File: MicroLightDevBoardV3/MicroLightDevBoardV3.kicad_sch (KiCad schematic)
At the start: 34 parts, among them J1 TYPE-C-31-M-12, J3 Conn_01x03_Socket, J4 Conn_01x01_Socket, J5 Conn_01x01_Socket, J6 Conn_01x04_Socket, SW1 SW_Push, U1 USBLC6-2P6, U2 STM32C071GBUx, U3 BQ25180, U4 S-85S1AB33-I6T1U, U5 DF53-2S-0.6H, U7 MC3479

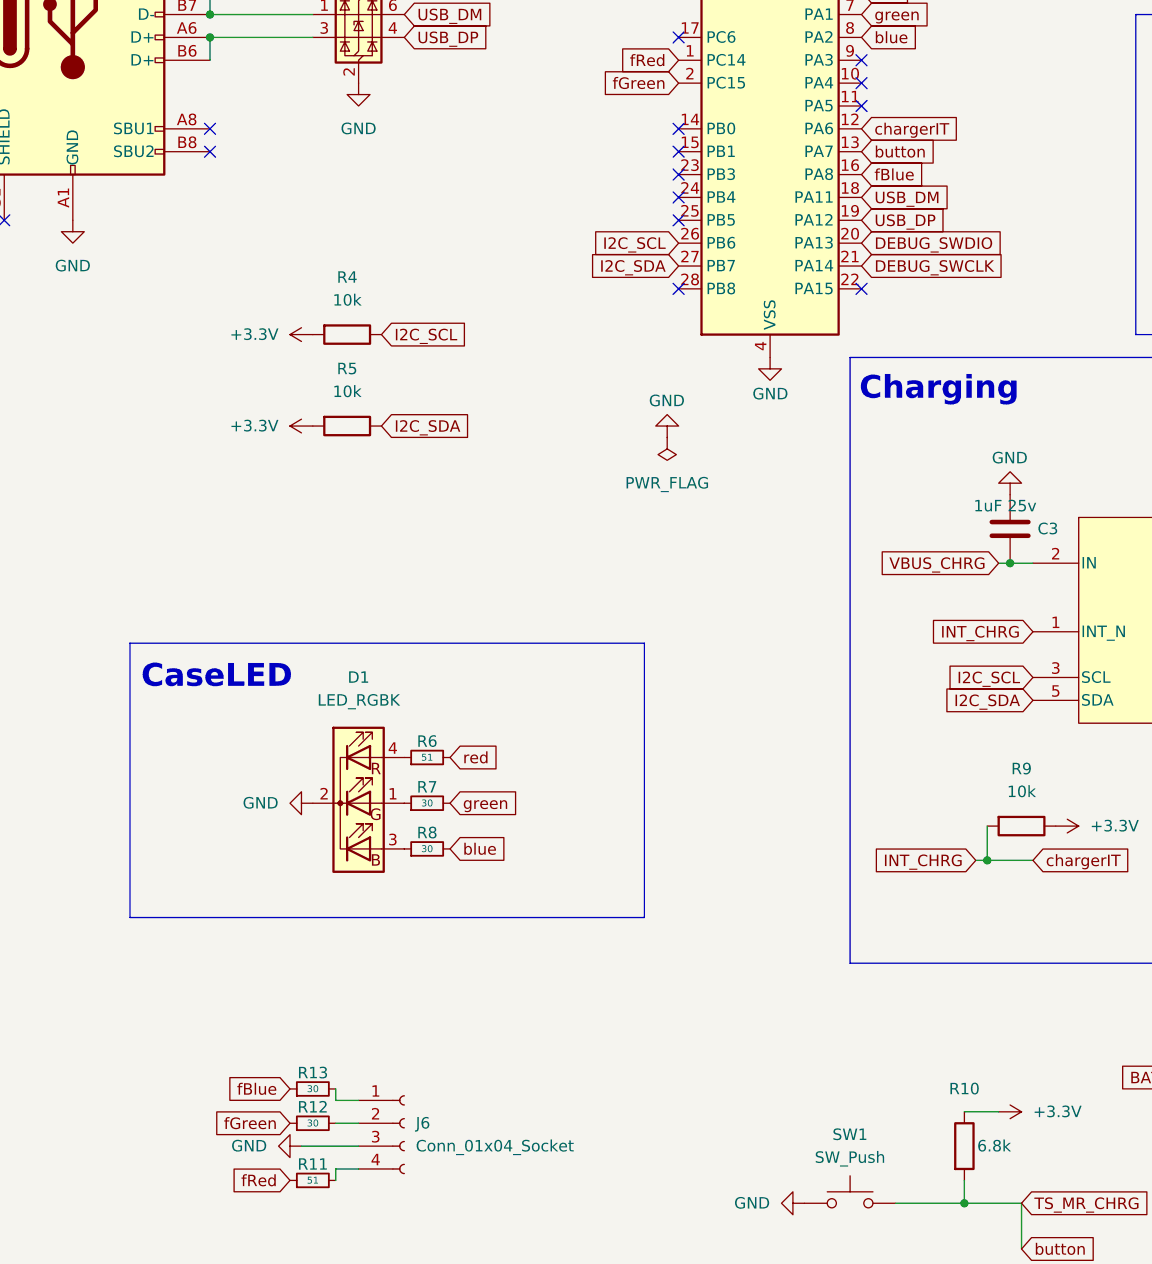
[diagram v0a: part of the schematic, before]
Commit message: rename fBlue to fBlueBulb as it controls power for blue in rgb led, as well as power for 2 pin bulb leds
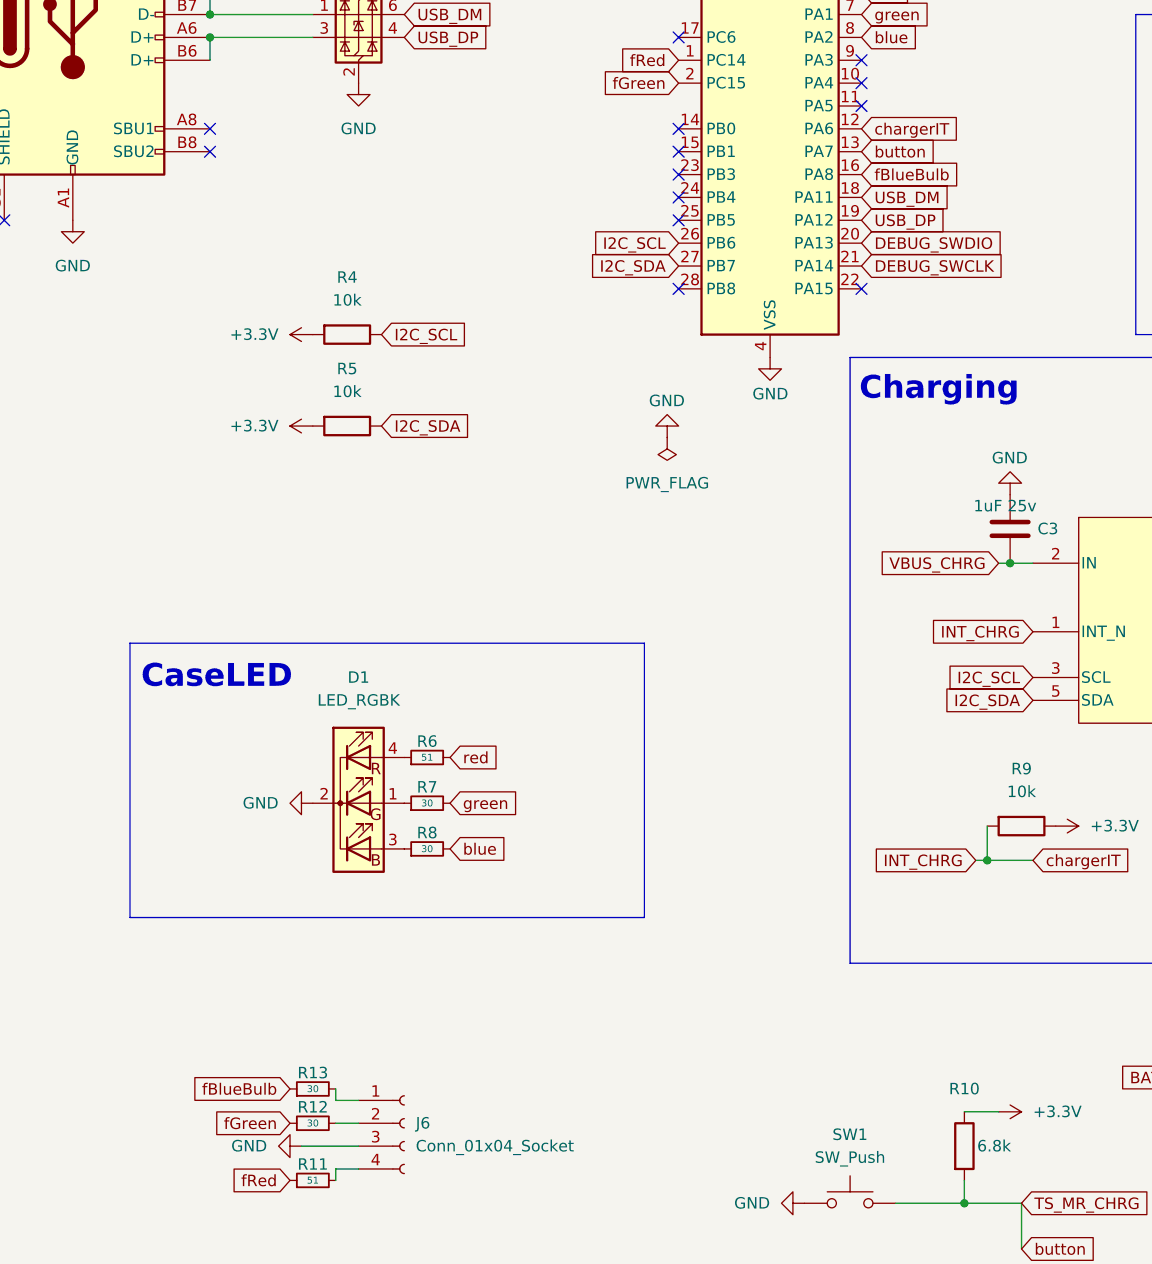
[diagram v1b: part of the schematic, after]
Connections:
- net fBlue renamed fBlueBulb
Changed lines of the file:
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@@
 		)
 	)
-	(global_label "fBlue"
+	(global_label "fBlueBulb"
 		(shape input)
 		(at 114.3 58.42 0)
@@
 		)
 		(property "Intersheetrefs" "${INTERSHEET_REFS}"
-			(at 122.1837 58.42 0)
+			(at 126.4169 58.42 0)
 			(effects
 				(font
@@
 		)
 	)
-	(global_label "fBlue"
+	(global_label "fBlueBulb"
 		(shape input)
 		(at 50.8 160.02 180)
@@
 		)
 		(property "Intersheetrefs" "${INTERSHEET_REFS}"
-			(at 42.9163 160.02 0)
+			(at 38.6831 160.02 0)
 			(effects
 				(font

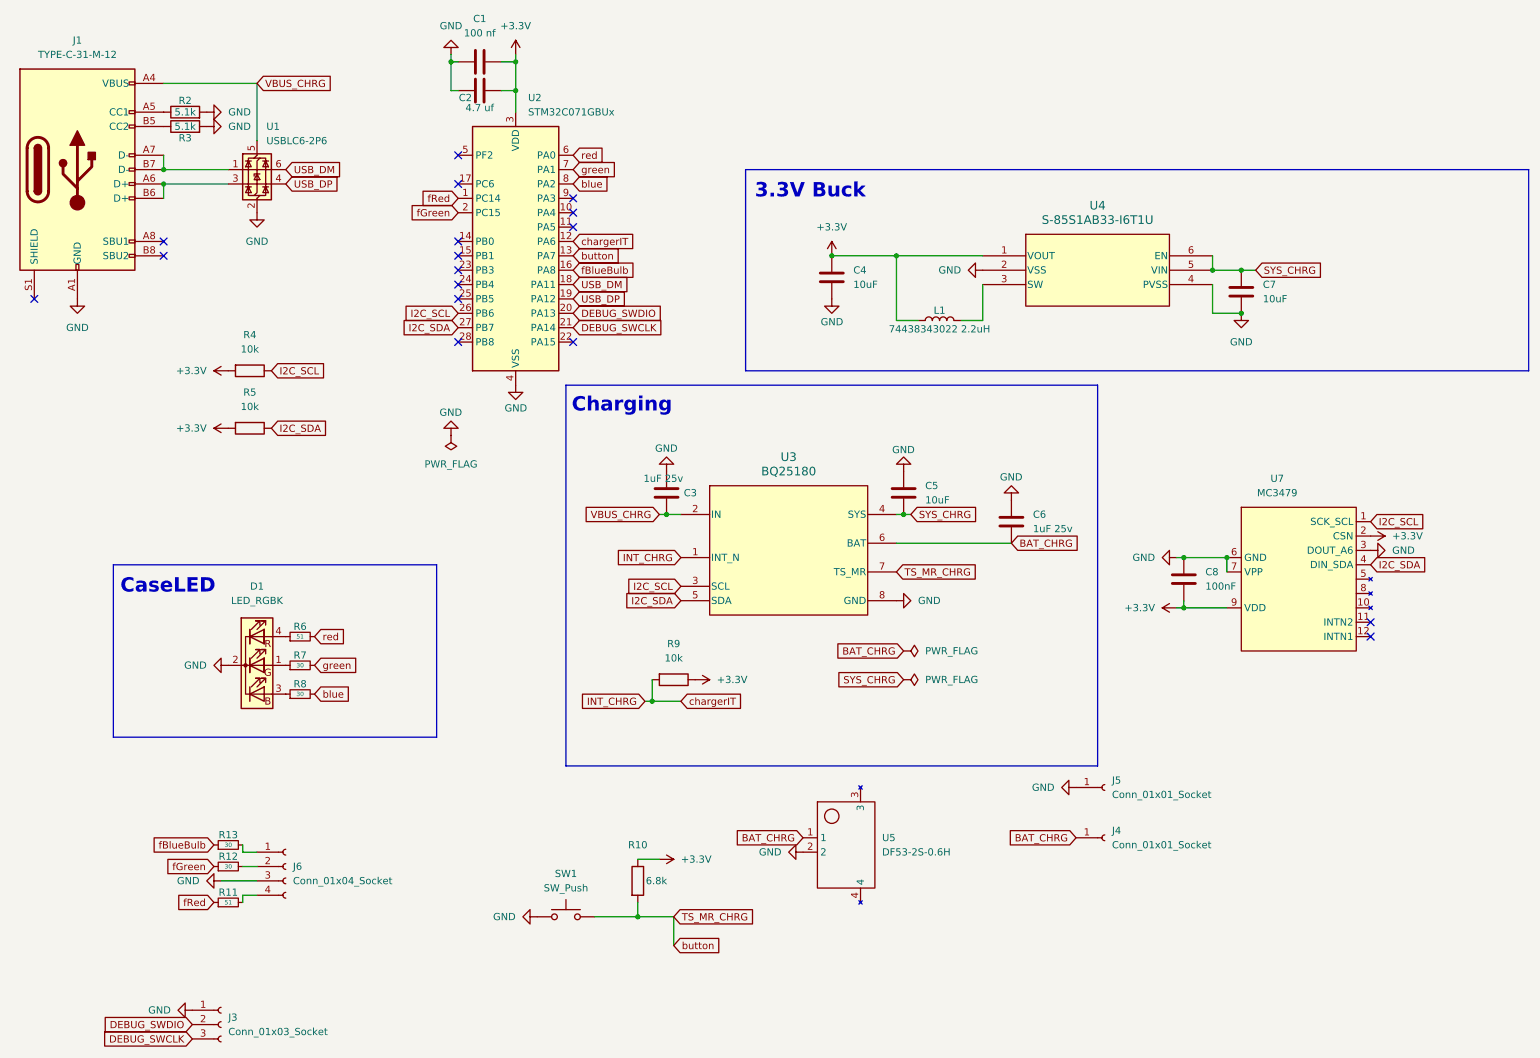
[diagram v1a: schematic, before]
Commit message: PCB battery connector, silkscreen, manufacturing changes / Firmware cleanup (#16)
* datasheet misunderstood, charger ic only prevents maximum sys voltage from vin. Using default of 4.5v

* refactor chip_state to move where state is stored. also pass milliseconds in to task instead of calculating and removed associated dependency

* changed error handling in DI layer

* improved labeling on kicad schematic

* update battery connector symbols, attempting to do male connector and wire/crimp assembly

* moved and made battery wire clip slightly smaller

* cleanup and silk screen resizing. Also added James Hunt and v1 silkscreen labels

* add edge cut instructions, add battery connector assembly instructions

* fixing up naming, bom exclusions, made debug pin pad size consistent with other through hole pads

* made debug area a bit smaller at the edges
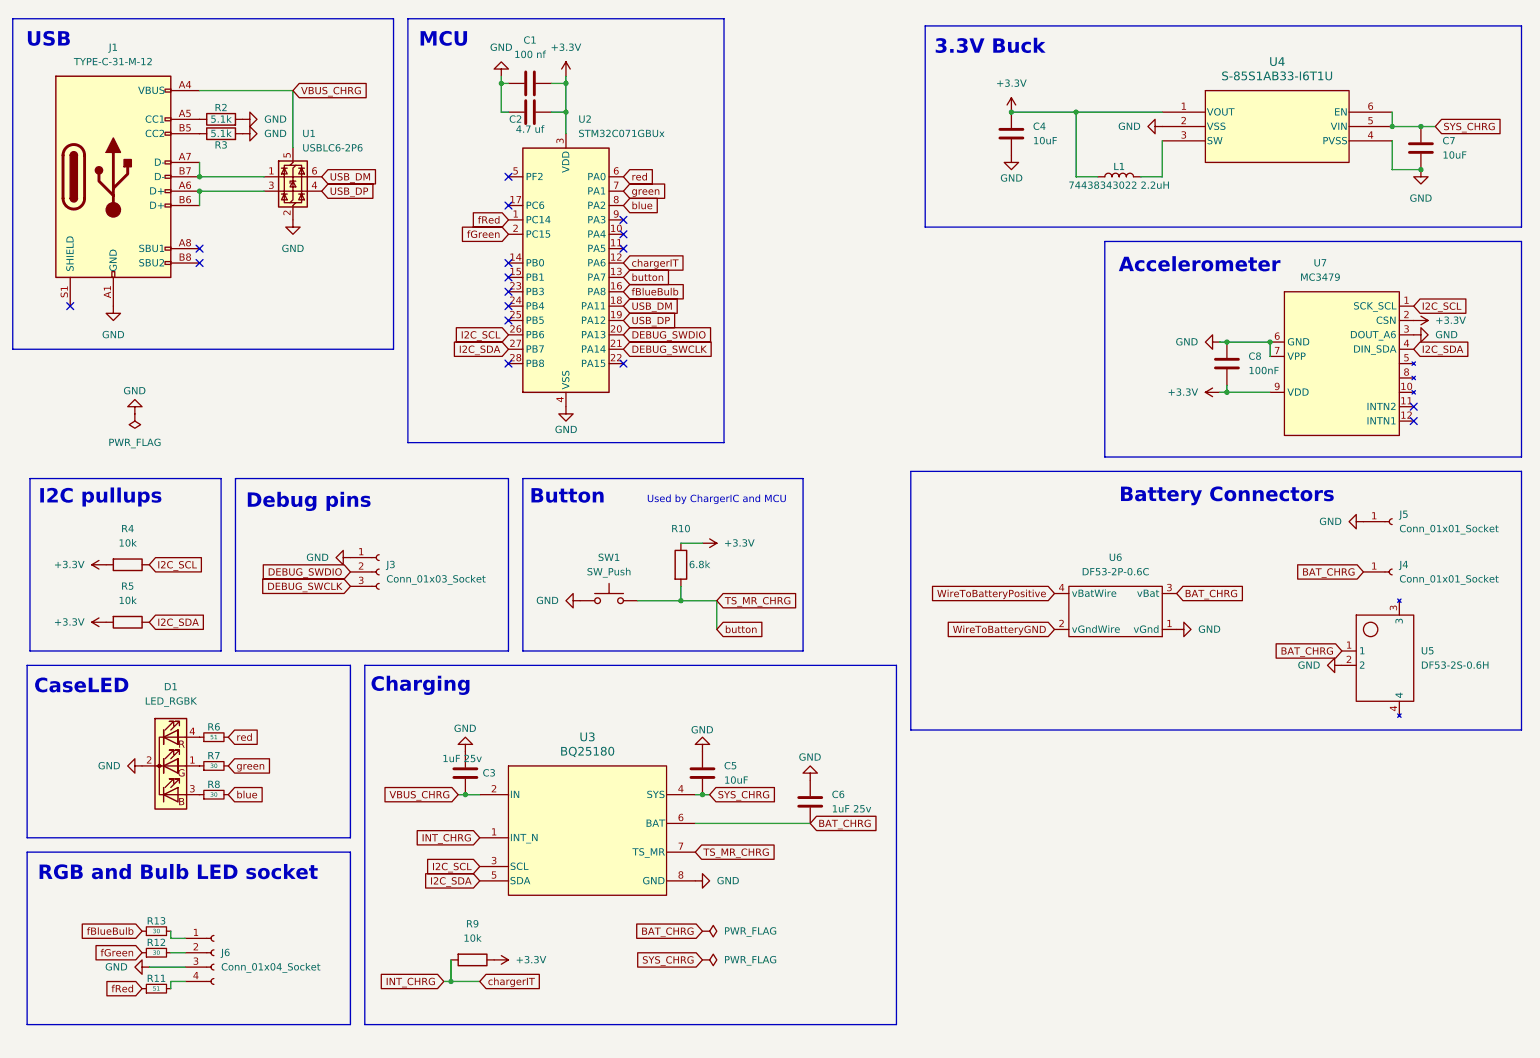
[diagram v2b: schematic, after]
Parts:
- added U6: DF53-2P-0.6C, symbol MicroLightDevBoard:DF53-2P-0.6C
- J3: footprint MicroLightDevBoard:PinSocket_1x03_P2.54mm_Vertical_debug -> MicroLightDevBoard:Microlight_debug_pins; now left out of the parts list
- J4, J5: now left out of the parts list
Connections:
- net BAT_CHRG: now also U6.3 (vBat)
- net GND: now also U6.1 (vGnd)
- new net WireToBatteryGND: U6.2 (vGndWire)
- new net WireToBatteryPositive: U6.4 (vBatWire)
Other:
- note added: "Accelerometer"
- note added: "Battery Connectors"
- note added: "Button"
- note added: "Debug pins"
- note added: "I2C pullups"
- note added: "MCU"
- note added: "RGB and Bulb LED socket"
- note added: "USB"
- note added: "Used by ChargerIC and MCU"
- moved on the sheet: C1, C2, C3, C4, C5, C6, C7, C8, D1, J1, J3, J4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

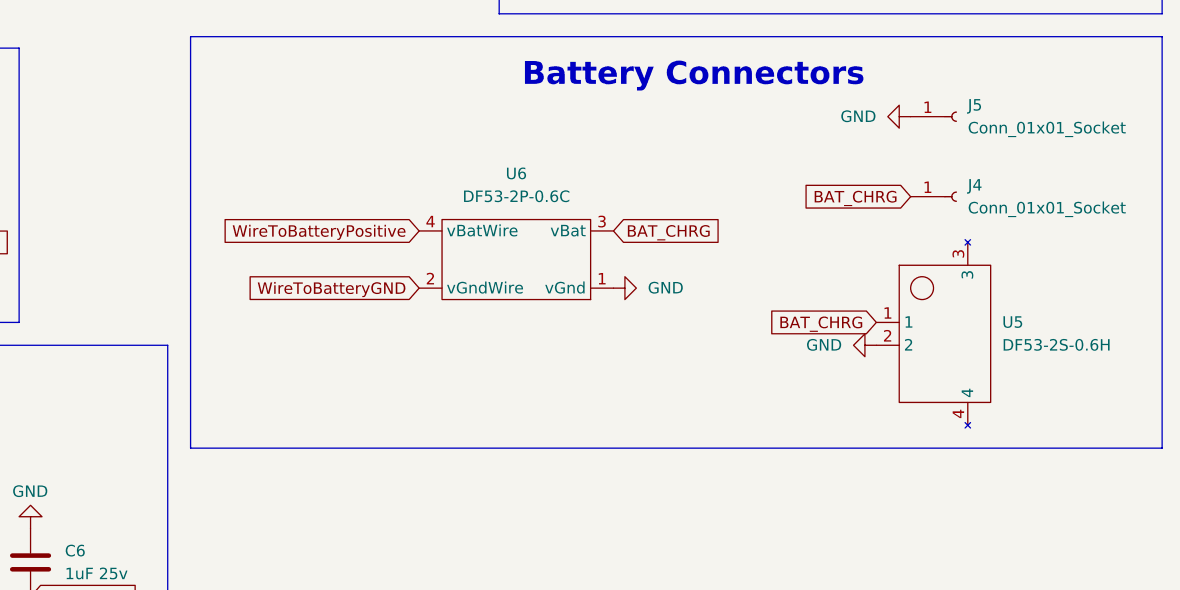
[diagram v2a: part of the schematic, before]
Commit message: deleted battery pcb connector. moved button and case led closer to usb
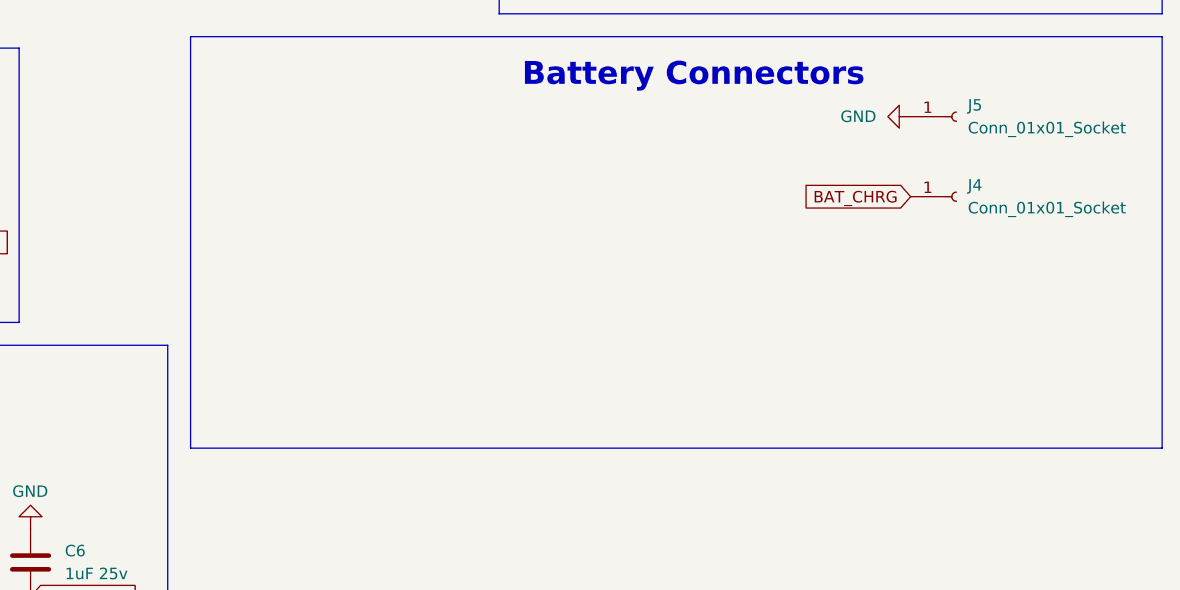
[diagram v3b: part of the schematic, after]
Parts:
- removed U5: DF53-2S-0.6H, MicroLightDevBoard:DF53-2S-0.6H, symbol MicroLightDevBoard:DF53-2S-0.6H
- removed U6: DF53-2P-0.6C, symbol MicroLightDevBoard:DF53-2P-0.6C

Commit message: improve front led pads
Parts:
- J6: footprint Connector_PinSocket_1.27mm:PinSocket_1x04_P1.27mm_Vertical -> MicroLightDevBoard:rgbLed4Pin_1.27mm
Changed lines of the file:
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@@
 			)
 		)
-		(property "Footprint" "Connector_PinSocket_1.27mm:PinSocket_1x04_P1.27mm_Vertical"
+		(property "Footprint" "MicroLightDevBoard:rgbLed4Pin_1.27mm"
 			(at 50.8 179.07 0)
 			(effects
